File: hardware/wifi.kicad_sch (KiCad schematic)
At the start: 29 parts, among them J1 RJ45_Hanrun_HR913550A_Horizon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, U3 AP6212, Y1 26MHz

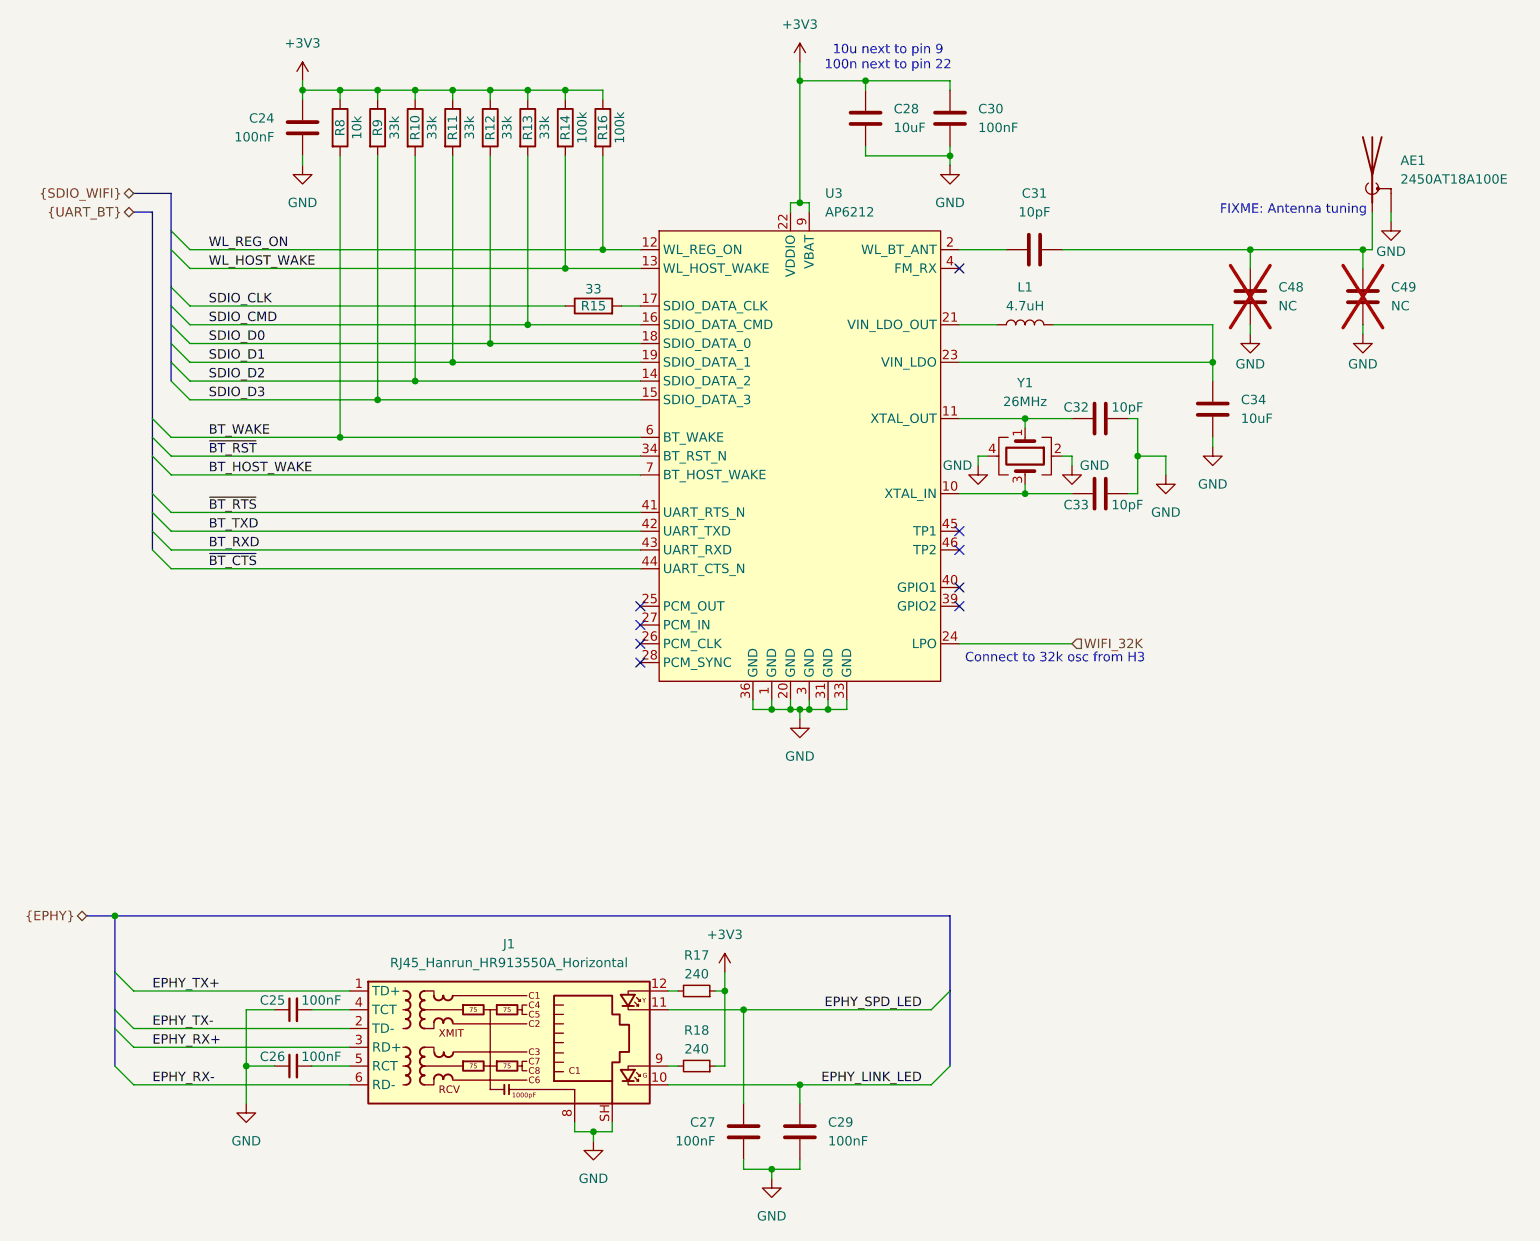
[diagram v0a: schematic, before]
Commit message: Finished DC DC converters and started decoupling the CPU
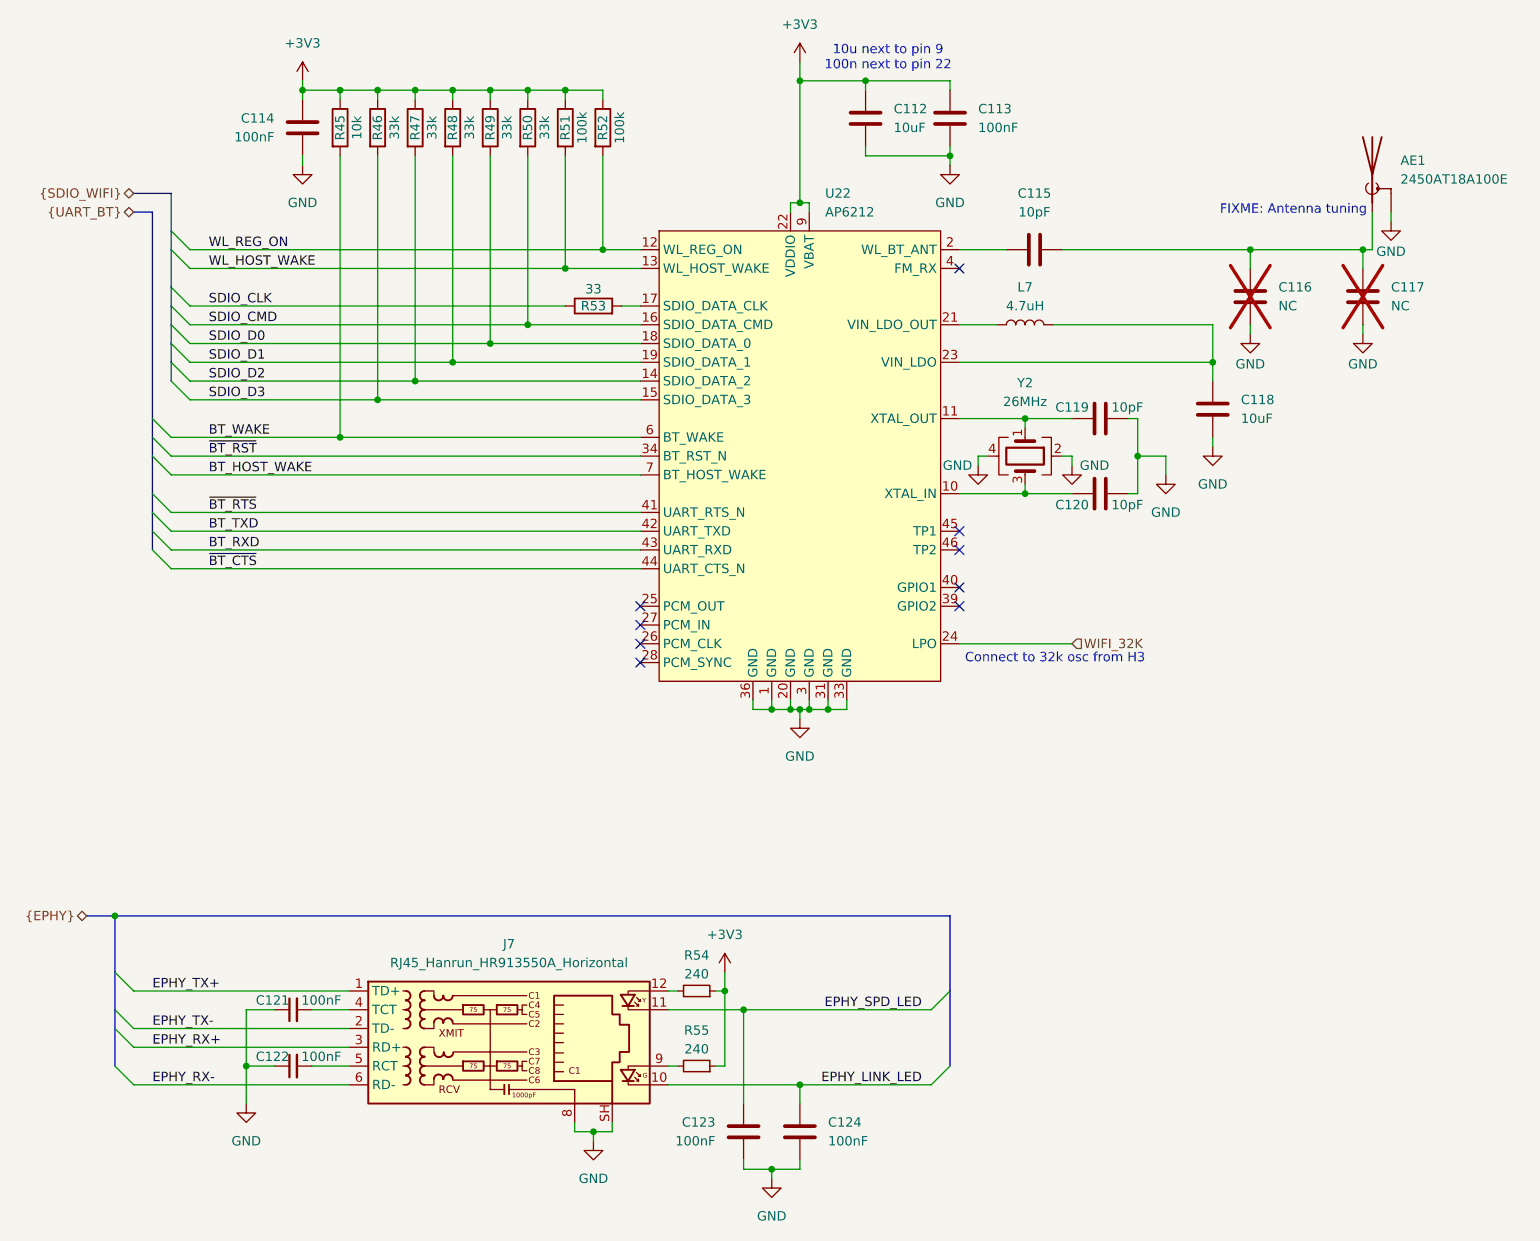
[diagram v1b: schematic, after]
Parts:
- renumbered C28 to C112, C30 to C113, C24 to C114, C31 to C115, C48 to C116, C49 to C117, C34 to C118, C32 to C119, C33 to C120, C25 to C121, C26 to C122, C27 to C123, C29 to C124, J1 to J7, L1 to L7, R8 to R45, R9 to R46, R10 to R47, R11 to R48, R12 to R49, R13 to R50, R14 to R51, R16 to R52, R15 to R53, R17 to R54, R18 to R55, U3 to U22, Y1 to Y2

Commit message: Decoupling on PCB side almost done
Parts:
- added R69, R70: 100k, Resistor_SMD:R_0402_1005Metric, symbol Device:R
- C116, C117: LCSC Part # C32949 -> (none)
- J7: FT Rotation Offset (none) -> 180
- L7: value 4.7uH -> 2.2uH; footprint (none) -> Inductor_SMD:L_Sunlord_SWPA3015S; LCSC Part # (none) -> C19734
- R51: value 100k -> 10k; LCSC Part # C25741 -> C25744
- R53: LCSC Part # (none) -> C25105
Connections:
- net +3V3: no longer C112.1, C113.1, C114.1, R45.1, R46.1, R47.1, R48.1, R49.1, R50.1, R51.1, R52.1, U22.22 (VDDIO), U22.9 (VBAT)
- net BT_WAKE: now also R69.1
- net GND: now also R52.2, R69.2, R70.2
- net WIFI_32K: now also R51.2
- net WL_HOST_WAKE: no longer R51.2
- net WL_REG_ON: now also R52.1; no longer R52.2
- net ~{BT_RST}: now also R70.1
- new net +3V3_WIFI: C112.1, C113.1, C114.1, R45.1, R46.1, R47.1, R48.1, R49.1, R50.1, R51.1, U22.22 (VDDIO), U22.9 (VBAT)
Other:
- moved on the sheet: R52

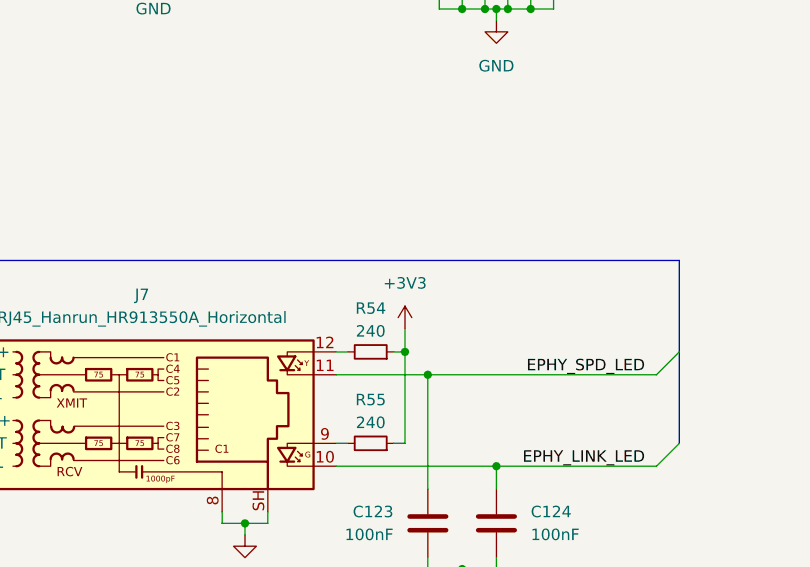
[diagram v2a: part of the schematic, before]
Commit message: Routed DCDC, EPHY and SD
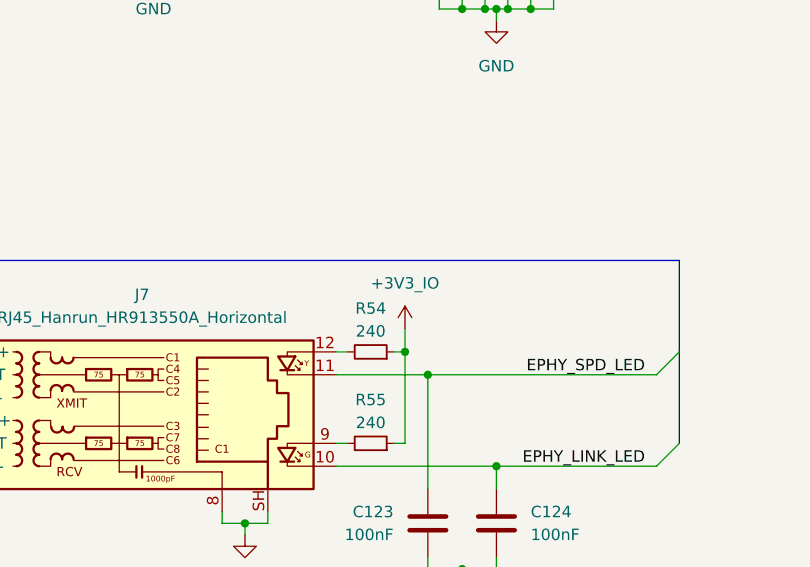
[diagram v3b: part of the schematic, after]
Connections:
- net +3V3 renamed +3V3_IO
